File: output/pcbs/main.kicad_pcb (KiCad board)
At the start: 2 copper layers, 141 x 130.1 mm, 60 parts

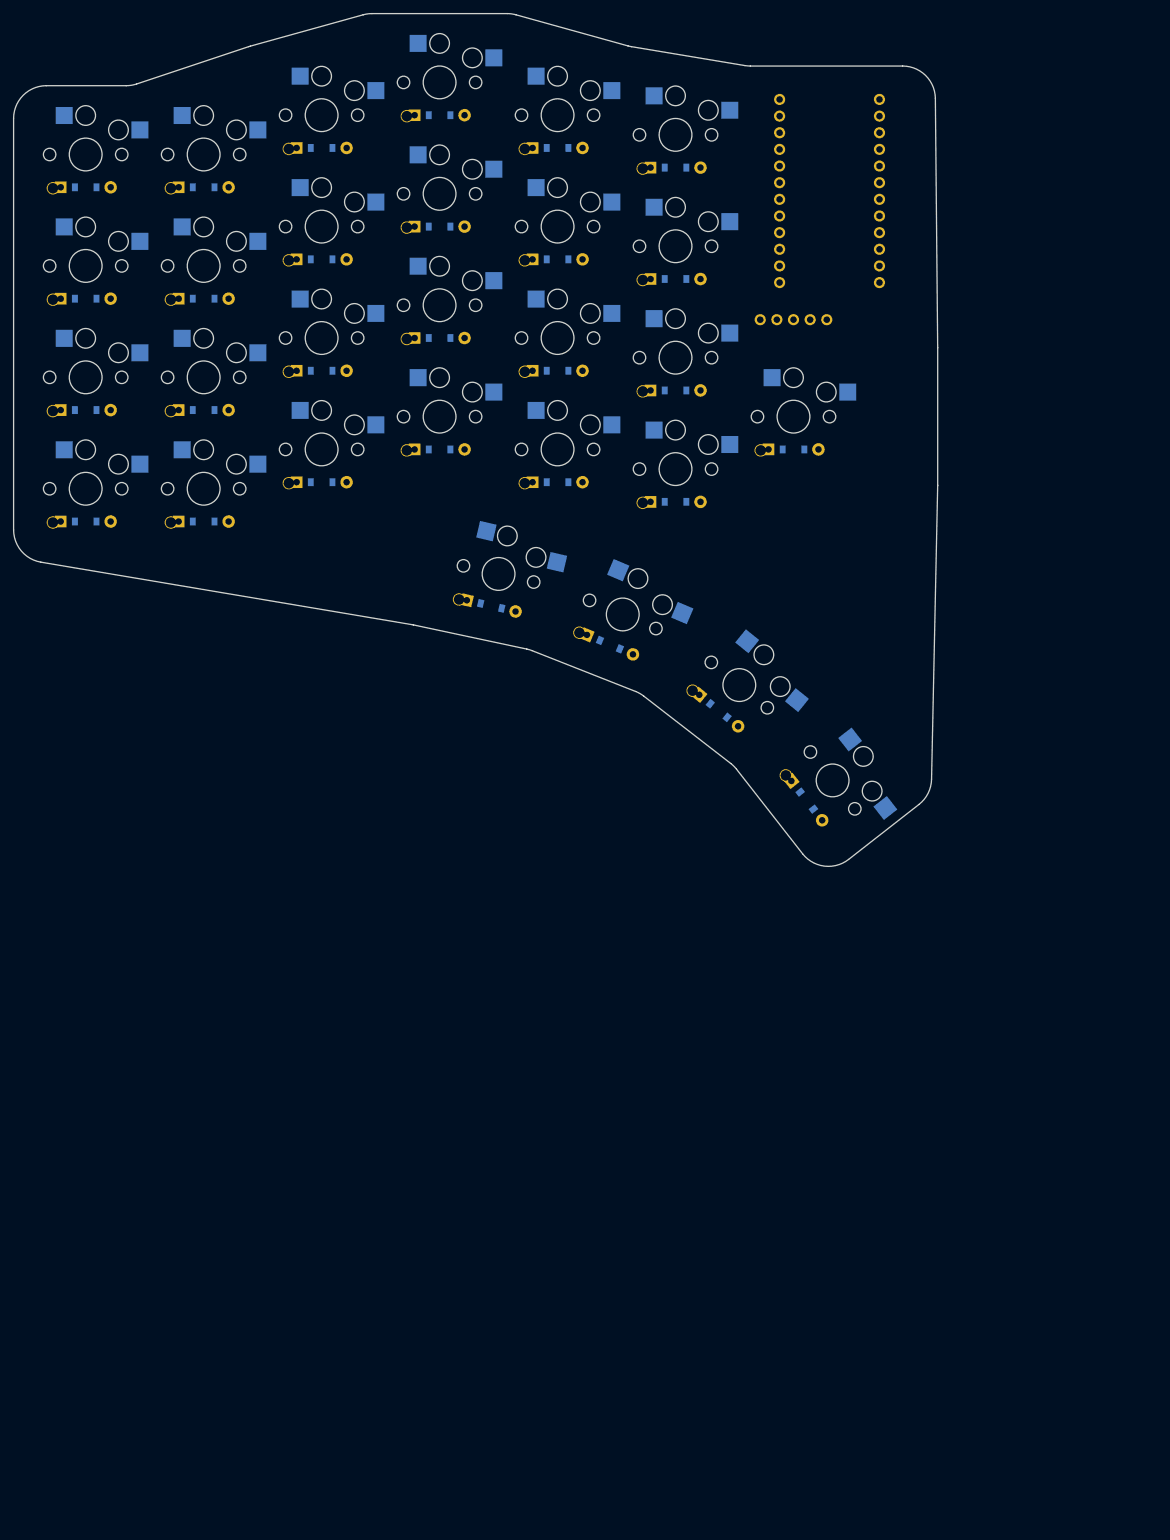
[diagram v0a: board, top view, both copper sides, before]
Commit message: Position board at top-left of A3 sheet working area
Add an anchor shift ([26, -87.5]) to the root 'main' zone so the whole board
(points, outlines, footprints all cascade from it) is translated as a rigid
unit to sit at the top-left of the A3 drawing sheet (~15mm inset), so it opens
properly placed in KiCad. Board bbox is now X:15..156 Y:15..145, comfortably
within the A3 frame. Pure translation; geometry and wiring unchanged.
Regenerated output/.
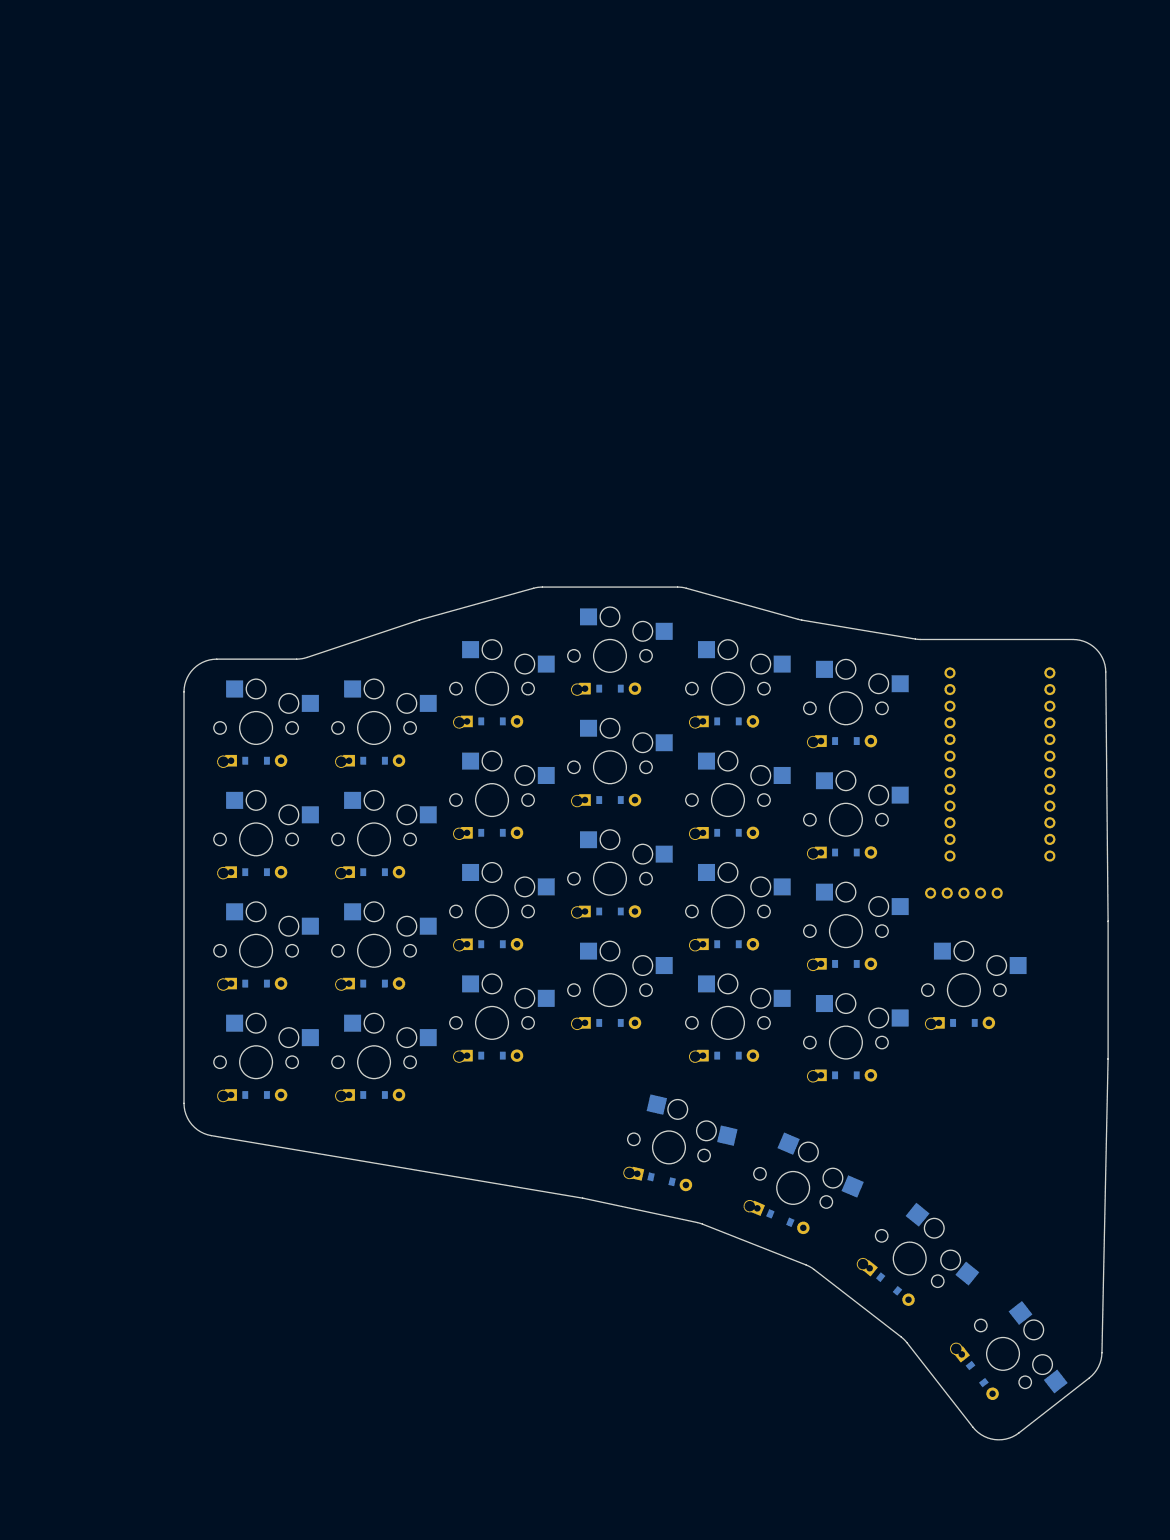
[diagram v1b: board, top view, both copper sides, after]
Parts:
- moved D1 91.3 mm to (26.0, 92.5)
- moved D10 91.3 mm to (62.0, 69.5)
- moved D11 91.3 mm to (62.0, 52.5)
- moved D12 91.3 mm to (62.0, 35.5)
- moved D13 91.3 mm to (80.0, 81.5)
- moved D14 91.3 mm to (80.0, 64.5)
- moved D15 91.3 mm to (80.0, 47.5)
- moved D16 91.3 mm to (80.0, 30.5)
- moved D17 91.3 mm to (98.0, 86.5)
- moved D18 91.3 mm to (98.0, 69.5)
- moved D19 91.3 mm to (98.0, 52.5)
- moved D2 91.3 mm to (26.0, 75.5)
- moved D20 91.3 mm to (98.0, 35.5)
- moved D21 91.3 mm to (116.0, 89.5)
- moved D22 91.3 mm to (116.0, 72.5)
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
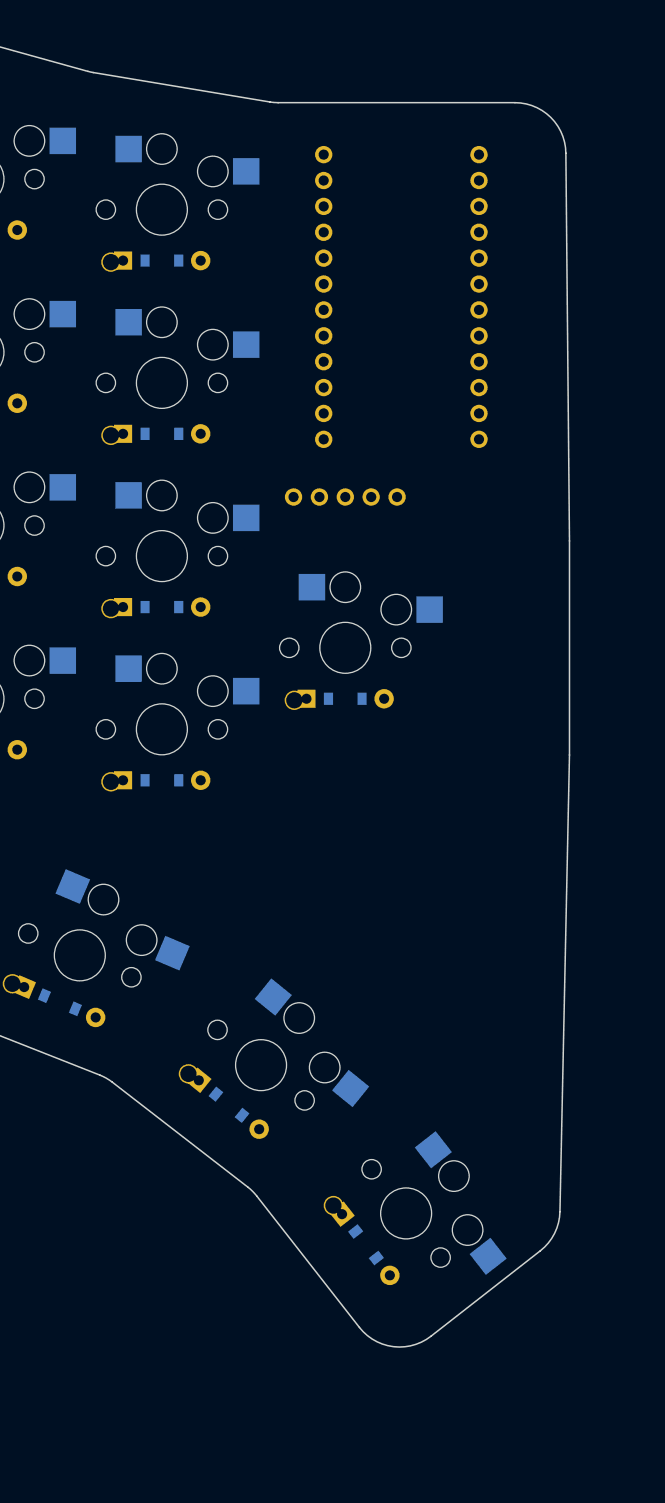
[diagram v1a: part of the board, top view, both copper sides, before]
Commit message: Add Panasonic EVQWGD001 rotary encoders (x2)
- Add KiCad 8 (footprint syntax) port of the EVQWGD001 scroll encoder
  footprint (converted from the legacy ergogen 'scrollwheel' module footprint)
  at footprints/ceoloide/encoder_evqwgd001.js
- Place two encoders on the Back side with placeholder positions (adjust
  where: to taste)
- Wire rotary A/C to free nice!nano pins P0/P1 (ENC1) and P2/P10 (ENC2);
  B/D and push-switch tied to GND for now
- Regenerated output/
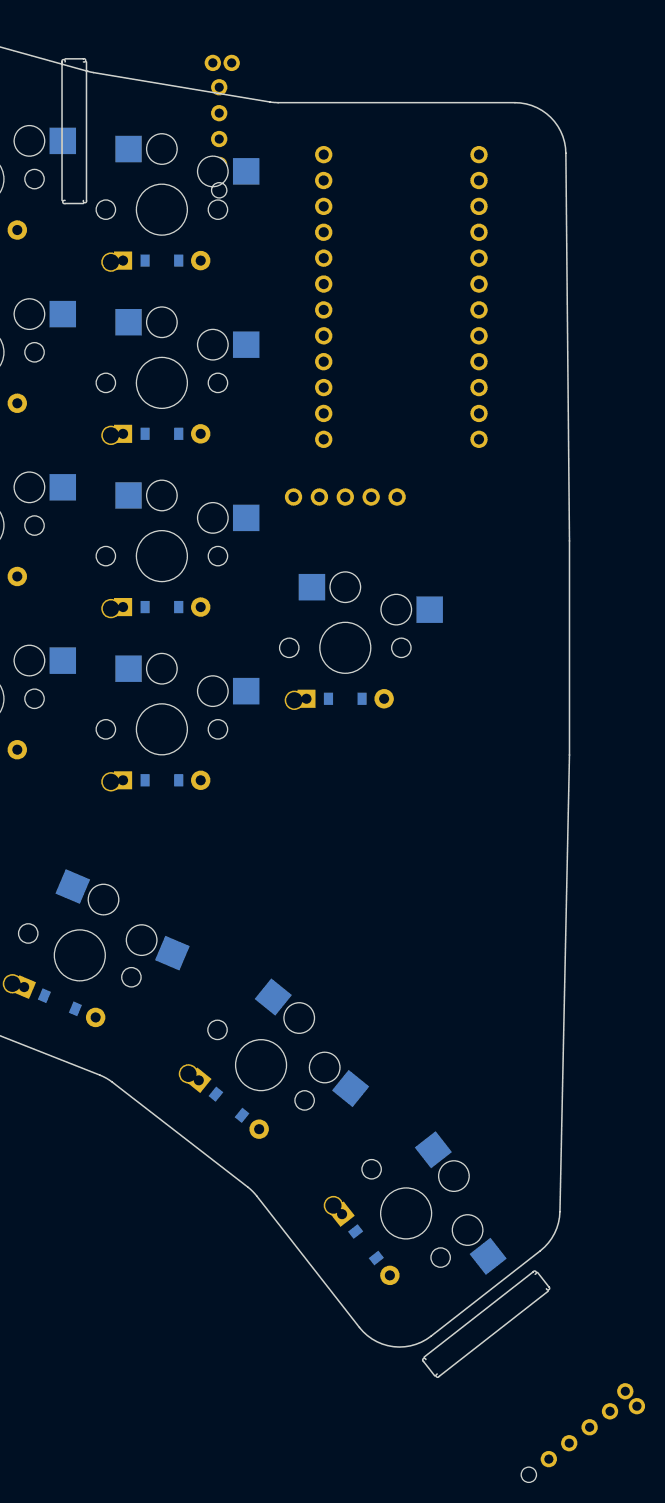
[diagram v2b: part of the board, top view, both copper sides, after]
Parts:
- added ENC1: , ceoloide:encoder_evqwgd001, B.Cu at (153.5, 149.3)
- added ENC2: , ceoloide:encoder_evqwgd001, B.Cu at (116.0, 25.3)
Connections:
- MCU1 pad 1: P1 -> ENC1_C
- MCU1 pad 13: P10 -> ENC2_C
- MCU1 pad 2: P0 -> ENC1_A
- MCU1 pad 5: P2 -> ENC2_A
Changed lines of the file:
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@@
 (net 52 "RAW")
 (net 53 "RST")
-(net 54 "P10")
-(net 55 "P1")
-(net 56 "P0")
-(net 57 "P2")
+(net 54 "ENC2_C")
+(net 55 "ENC1_C")
+(net 56 "ENC1_A")
+(net 57 "ENC2_A")
 (net 58 "P101")
 (net 59 "P102")
@@
     (fp_line (start -8.89 16.57) (end 8.89 16.57) (layer "Dwgs.User") (stroke (width 0.15) (type solid)))
     (pad "24" thru_hole circle (at -7.62 -12.7 0) (size 1.7 1.7) (drill 1) (layers "*.Cu" "*.Mask") (net 52 "RAW"))
-    (pad "1" thru_hole circle (at 7.62 -12.7 0) (size 1.7 1.7) (drill 1) (layers "*.Cu" "*.Mask") (net 55 "P1"))
-    (fp_text user "P1" (at 4.47 -12.7 0) (layer "B.SilkS")
+    (pad "1" thru_hole circle (at 7.62 -12.7 0) (size 1.7 1.7) (drill 1) (layers "*.Cu" "*.Mask") (net 55 "ENC1_C"))
+    (fp_text user "ENC1_C" (at 4.47 -12.7 0) (layer "B.SilkS")
       (effects (font (size 1 1) (thickness 0.15)) (justify mirror))
     )
@@
     )
     (pad "23" thru_hole circle (at -7.62 -10.16 0) (size 1.7 1.7) (drill 1) (layers "*.Cu" "*.Mask") (net 3 "GND"))
-    (pad "2" thru_hole circle (at 7.62 -10.16 0) (size 1.7 1.7) (drill 1) (layers "*.Cu" "*.Mask") (net 56 "P0"))
-    (fp_text user "P0" (at 4.47 -10.16 0) (layer "B.SilkS")
+    (pad "2" thru_hole circle (at 7.62 -10.16 0) (size 1.7 1.7) (drill 1) (layers "*.Cu" "*.Mask") (net 56 "ENC1_A"))
+    (fp_text user "ENC1_A" (at 4.47 -10.16 0) (layer "B.SilkS")
       (effects (font (size 1 1) (thickness 0.15)) (justify mirror))
     )
@@
     )
     (pad "20" thru_hole circle (at -7.62 -2.539999999999999 0) (size 1.7 1.7) (drill 1) (layers "*.Cu" "*.Mask") (net 1 "P21"))
-    (pad "5" thru_hole circle (at 7.62 -2.539999999999999 0) (size 1.7 1.7) (drill 1) (layers "*.Cu" "*.Mask") (net 57 "P2"))
-    (fp_text user "P2" (at 4.47 -2.539999999999999 0) (layer "B.SilkS")
+    (pad "5" thru_hole circle (at 7.62 -2.539999999999999 0) (size 1.7 1.7) (drill 1) (layers "*.Cu" "*.Mask") (net 57 "ENC2_A"))
+    (fp_text user "ENC2_A" (at 4.47 -2.539999999999999 0) (layer "B.SilkS")
       (effects (font (size 1 1) (thickness 0.15)) (justify mirror))
     )
@@
       (effects (font (size 1 1) (thickness 0.15)) (justify mirror))
     )
-    (pad "13" thru_hole circle (at -7.62 15.240000000000002 0) (size 1.7 1.7) (drill 1) (layers "*.Cu" "*.Mask") (net 54 "P10"))
+    (pad "13" thru_hole circle (at -7.62 15.240000000000002 0) (size 1.7 1.7) (drill 1) (layers "*.Cu" "*.Mask") (net 54 "ENC2_C"))
     (pad "12" thru_hole circle (at 7.62 15.240000000000002 0) (size 1.7 1.7) (drill 1) (layers "*.Cu" "*.Mask") (net 45 "SCK"))
     (fp_text user "SCK" (at 4.47 15.240000000000002 0) (layer "B.SilkS")
       (effects (font (size 1 1) (thickness 0.15)) (justify mirror))
     )
-    (fp_text user "P10" (at -4.47 15.240000000000002 0) (layer "B.SilkS")
+    (fp_text user "ENC2_C" (at -4.47 15.240000000000002 0) (layer "B.SilkS")
       (effects (font (size 1 1) (thickness 0.15)) (justify mirror))
     )
@@
     (fp_line (start 8.95 -11.43) (end 6.29 -11.43) (layer "B.SilkS") (stroke (width 0.12) (type solid)))
   )
+  (footprint "ceoloide:encoder_evqwgd001"
+    (layer "B.Cu")
+    (at 153.51322950000002 149.3410483 -52)
+    (property "Reference" "ENC1"
+      (at 0 0 -52)
+      (layer "B.SilkS")
+      hide
+      (effects (font (size 1 1) (thickness 0.15)))
+    )
+    (attr through_hole)
+    (fp_line (start -8.4 -6.4) (end 8.4 -6.4) (layer "Dwgs.User") (stroke (width 0.12) (type solid)))
+    (fp_line (start 8.4 -6.4) (end 8.4 7.4) (layer "Dwgs.User") (stroke (width 0.12) (type solid)))
+    (fp_line (start 8.4 7.4) (end -8.4 7.4) (layer "Dwgs.User") (stroke (width 0.12) (type solid)))
+    (fp_line (start -8.4 7.4) (end -8.4 -6.4) (layer "Dwgs.User") (stroke (width 0.12) (type solid)))
+      (fp_line (start -9.8 7.3) (end -9.8 -6.3) (layer "Edge.Cuts") (stroke (width 0.15) (type solid)))
+      (fp_line (start -7.4 -6.3) (end -7.4 7.3) (layer "Edge.Cuts") (stroke (width 0.15) (type solid)))
+      (fp_line (start -9.5 -6.6) (end -7.7 -6.6) (layer "Edge.Cuts") (stroke (width 0.15) (type solid)))
+      (fp_line (start -7.7 7.6) (end -9.5 7.6) (layer "Edge.Cuts") (stroke (width 0.15) (type solid)))
+      (fp_arc (start -7.7 7.3) (mid -7.4878 7.5121) (end -7.4 7.3) (layer "Edge.Cuts") (stroke (width 0.15) (type solid)))
+      (fp_arc (start -9.5 7.3) (mid -9.7121 7.5121) (end -9.5 7.6) (layer "Edge.Cuts") (stroke (width 0.15) (type solid)))
+      (fp_arc (start -7.7 -6.3) (mid -7.4878 -6.5121) (end -7.7 -6.6) (layer "Edge.Cuts") (stroke (width 0.15) (type solid)))
+      (fp_arc (start -9.5 -6.3) (mid -9.7121 -6.5121) (end -9.8 -6.3) (layer "Edge.Cuts") (stroke (width 0.15) (type solid)))
+      (pad "1" thru_hole circle (at 6.85 -6.2 -52) (size 1.6 1.6) (drill 0.9) (layers "*.Cu" "*.Mask") (net 3 "GND"))
+      (pad "2" thru_hole circle (at 5 -6.2 -52) (size 1.6 1.6) (drill 0.9) (layers "*.Cu" "*.Mask") (net 3 "GND"))
+      (pad "A" thru_hole circle (at 5.625 -3.81 -52) (size 1.6 1.6) (drill 0.9) (layers "*.Cu" "*.Mask") (net 56 "ENC1_A"))
+      (pad "B" thru_hole circle (at 5.625 -1.27 -52) (size 1.6 1.6) (drill 0.9) (layers "*.Cu" "*.Mask") (net 3 "GND"))
+      (pad "C" thru_hole circle (at 5.625 1.27 -52) (size 1.6 1.6) (drill 0.9) (layers "*.Cu" "*.Mask") (net 55 "ENC1_C"))
+      (pad "D" thru_hole circle (at 5.625 3.81 -52) (size 1.6 1.6) (drill 0.9) (layers "*.Cu" "*.Mask") (net 3 "GND"))
+      (pad "" np_thru_hole circle (at 5.625 6.3 -52) (size 1.5 1.5) (drill 1.5) (layers "*.Cu" "*.Mask"))
+  )
+  (footprint "ceoloide:encoder_evqwgd001"
+    (layer "B.Cu")
+    (at 116 25.3 0)
+    (property "Reference" "ENC2"
+      (at 0 0 0)
+      (layer "B.SilkS")
+      hide
+      (effects (font (size 1 1) (thickness 0.15)))
+    )
+    (attr through_hole)
+    (fp_line (start -8.4 -6.4) (end 8.4 -6.4) (layer "Dwgs.User") (stroke (width 0.12) (type solid)))
+    (fp_line (start 8.4 -6.4) (end 8.4 7.4) (layer "Dwgs.User") (stroke (width 0.12) (type solid)))
+    (fp_line (start 8.4 7.4) (end -8.4 7.4) (layer "Dwgs.User") (stroke (width 0.12) (type solid)))
+    (fp_line (start -8.4 7.4) (end -8.4 -6.4) (layer "Dwgs.User") (stroke (width 0.12) (type solid)))
+      (fp_line (start -9.8 7.3) (end -9.8 -6.3) (layer "Edge.Cuts") (stroke (width 0.15) (type solid)))
+      (fp_line (start -7.4 -6.3) (end -7.4 7.3) (layer "Edge.Cuts") (stroke (width 0.15) (type solid)))
+      (fp_line (start -9.5 -6.6) (end -7.7 -6.6) (layer "Edge.Cuts") (stroke (width 0.15) (type solid)))
+      (fp_line (start -7.7 7.6) (end -9.5 7.6) (layer "Edge.Cuts") (stroke (width 0.15) (type solid)))
+      (fp_arc (start -7.7 7.3) (mid -7.4878 7.5121) (end -7.4 7.3) (layer "Edge.Cuts") (stroke (width 0.15) (type solid)))
+      (fp_arc (start -9.5 7.3) (mid -9.7121 7.5121) (end -9.5 7.6) (layer "Edge.Cuts") (stroke (width 0.15) (type solid)))
+      (fp_arc (start -7.7 -6.3) (mid -7.4878 -6.5121) (end -7.7 -6.6) (layer "Edge.Cuts") (stroke (width 0.15) (type solid)))
+      (fp_arc (start -9.5 -6.3) (mid -9.7121 -6.5121) (end -9.8 -6.3) (layer "Edge.Cuts") (stroke (width 0.15) (type solid)))
+      (pad "1" thru_hole circle (at 6.85 -6.2 0) (size 1.6 1.6) (drill 0.9) (layers "*.Cu" "*.Mask") (net 3 "GND"))
+      (pad "2" thru_hole circle (at 5 -6.2 0) (size 1.6 1.6) (drill 0.9) (layers "*.Cu" "*.Mask") (net 3 "GND"))
+      (pad "A" thru_hole circle (at 5.625 -3.81 0) (size 1.6 1.6) (drill 0.9) (layers "*.Cu" "*.Mask") (net 57 "ENC2_A"))
+      (pad "B" thru_hole circle (at 5.625 -1.27 0) (size 1.6 1.6) (drill 0.9) (layers "*.Cu" "*.Mask") (net 3 "GND"))
+      (pad "C" thru_hole circle (at 5.625 1.27 0) (size 1.6 1.6) (drill 0.9) (layers "*.Cu" "*.Mask") (net 54 "ENC2_C"))
+      (pad "D" thru_hole circle (at 5.625 3.81 0) (size 1.6 1.6) (drill 0.9) (layers "*.Cu" "*.Mask") (net 3 "GND"))
+      (pad "" np_thru_hole circle (at 5.625 6.3 0) (size 1.5 1.5) (drill 1.5) (layers "*.Cu" "*.Mask"))
+  )
   (gr_line (start 15 93.77142847065225) (end 15 31) (layer Edge.Cuts) (stroke (width 0.15) (type default)))
